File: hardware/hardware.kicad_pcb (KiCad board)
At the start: 2 copper layers, 12 parts, among them J1 Conn_01x04_Male, J2 Teensy3.2, J3 DIN-5_180degree, J4 TeensyAudioShield3.2, J5 DIN-5_180degree, U1 6N139

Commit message: Prototype layout for pcb
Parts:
- moved J3 82.4 mm to (85.0, 77.0), turned to 270 degrees
- moved J1 78.2 mm to (90.0, 97.0)
- moved R1 71.0 mm to (78.0, 85.0), turned to 90 degrees
- moved D1 60.0 mm to (81.0, 109.0)
- moved R3 54.2 mm to (53.0, 124.0), turned to 180 degrees
- moved J5 53.5 mm to (85.0, 113.0), turned to 270 degrees
- moved R2 49.1 mm to (43.0, 120.0)
- moved R4 38.6 mm to (78.0, 111.0), turned to 270 degrees
- moved U1 37.0 mm to (85.0, 105.0), turned to 180 degrees
- moved J2 34.4 mm to (56.8, 121.9)
- moved J4 34.2 mm to (56.8, 90.7)
- moved C1 23.7 mm to (78.0, 129.0), turned to 90 degrees
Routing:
- net +5V: track 0.00 -> 87.9 mm
- net /MIDI_IN: track 0.00 -> 83.7 mm
- net /SDA: track 0.00 -> 81.0 mm
- net +3V3: track 0.00 -> 74.7 mm
- net /SCL: track 0.00 -> 70.3 mm
- net /SDCS: track 0.00 -> 32.6 mm
- net /SCK: track 0.00 -> 32.6 mm
- net /DOUT: track 0.00 -> 32.6 mm
- net /DIN: track 0.00 -> 32.5 mm
- net GNDA: track 0.00 -> 32.0 mm
- net GND: track 0.00 -> 32.0 mm
- net /Vol: track 0.00 -> 32.0 mm
- net /MOSI: track 0.00 -> 32.0 mm
- net /MISO: track 0.00 -> 32.0 mm
- net /MEMCS: track 0.00 -> 32.0 mm
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- added copper zone on B.Cu, net GND
- added copper zone on F.Cu, net GND
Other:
- board outline added: 60 x 59 mm

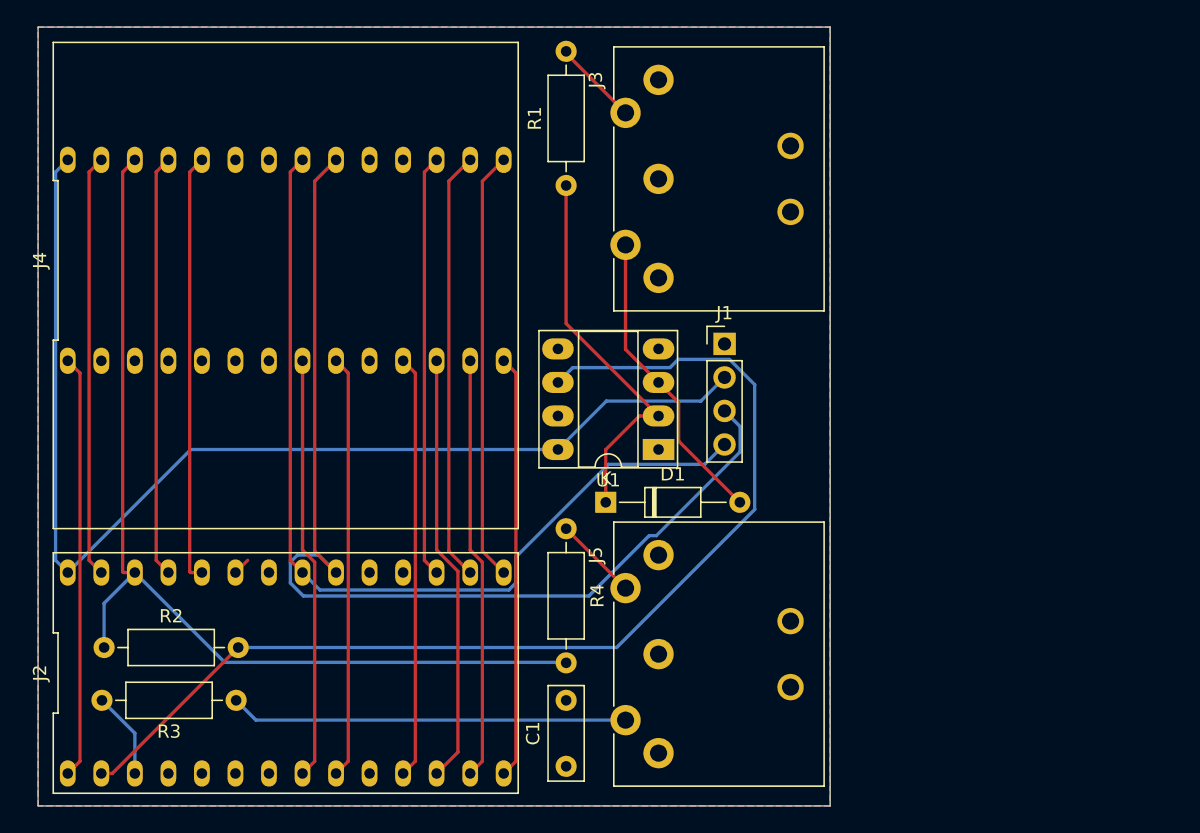
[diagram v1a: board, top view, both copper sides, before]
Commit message: Add some buttons and pots
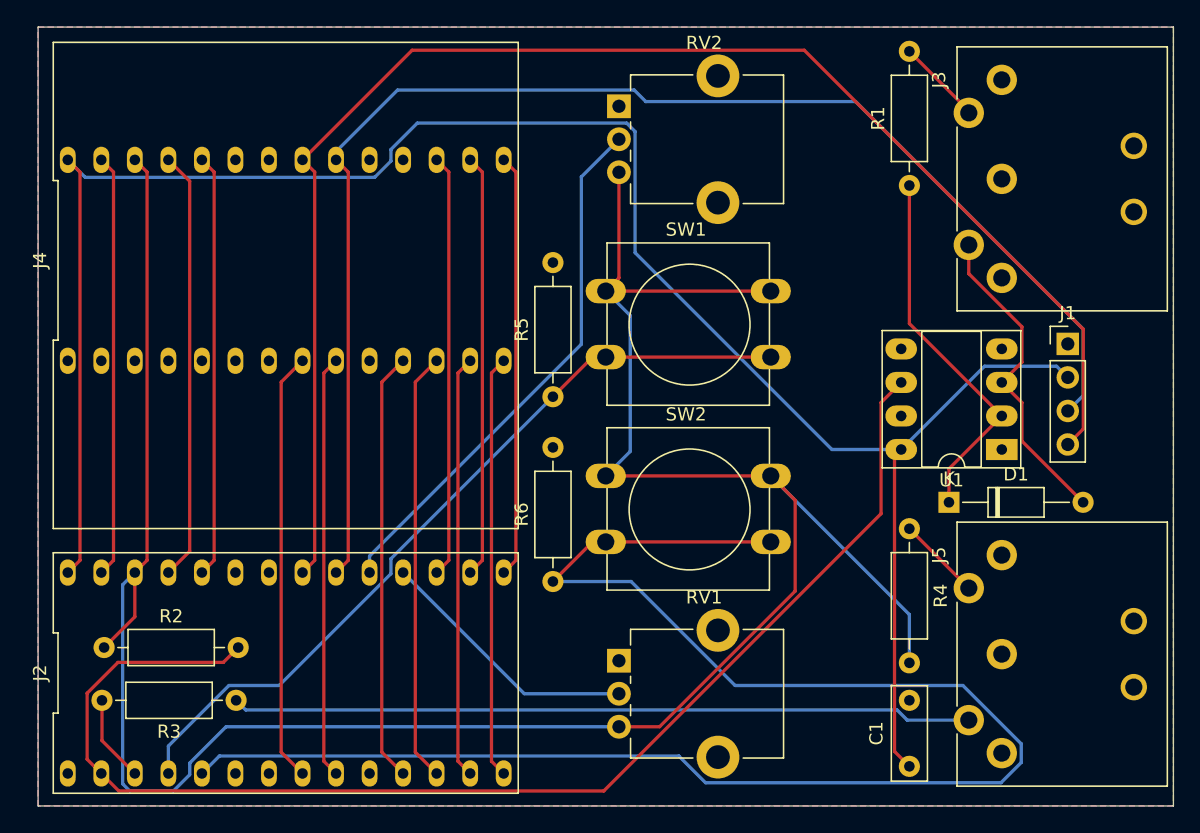
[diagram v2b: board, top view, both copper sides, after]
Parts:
- added R5: 10k, Resistor_THT:R_Axial_DIN0207_L6.3mm_D2.5mm_P10.16mm_Horizontal, F.Cu at (77.0, 101.0)
- added R6: 10k, Resistor_THT:R_Axial_DIN0207_L6.3mm_D2.5mm_P10.16mm_Horizontal, F.Cu at (77.0, 115.0)
- added RV1: R_POT, Potentiometer_THT:Potentiometer_Alpha_RD901F-40-00D_Single_Vertical_CircularHoles, F.Cu at (82.0, 121.0)
- added RV2: R_POT, Potentiometer_THT:Potentiometer_Alpha_RD901F-40-00D_Single_Vertical_CircularHoles, F.Cu at (82.0, 79.0)
- added SW1: SW_Push, Button_Switch_THT:SW_PUSH-12mm, F.Cu at (81.0, 93.0)
- added SW2: SW_Push, Button_Switch_THT:SW_PUSH-12mm, F.Cu at (81.0, 107.0)
- moved C1 26.0 mm to (104.0, 129.0)
- moved D1 26.0 mm to (107.0, 109.0)
- moved J1 26.0 mm to (116.0, 97.0)
- moved J3 26.0 mm to (111.0, 77.0)
- moved J5 26.0 mm to (111.0, 113.0)
- moved R1 26.0 mm to (104.0, 85.0)
- moved R4 26.0 mm to (104.0, 111.0)
- moved U1 26.0 mm to (111.0, 105.0)
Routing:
- net /D3: track 0.00 -> 123.8 mm
- net +3V3: track 74.7 -> 191.0 mm
- net +5V: track 87.9 -> 153.8 mm
- net /D2: track 0.00 -> 60.6 mm
- net /SCL: track 70.3 -> 112.6 mm
- net /A3: track 0.00 -> 40.6 mm
- net GND: track 32.0 -> 0.00 mm
- net Net-(J5-Pad5): track 30.1 -> 56.1 mm
- net /SDA: track 81.0 -> 105.4 mm
- net /A2: track 0.00 -> 20.2 mm
- net /MIDI_IN: track 83.7 -> 98.3 mm
- net /A7: track 1.31 -> 0.00 mm
- net Net-(D1-Pad2): track 23.1 -> 24.4 mm
- net Net-(D1-Pad1): track 29.4 -> 28.6 mm
- net /SCK: track 32.6 -> 32.0 mm
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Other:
- board size 60 x 59 mm -> 86 x 59 mm

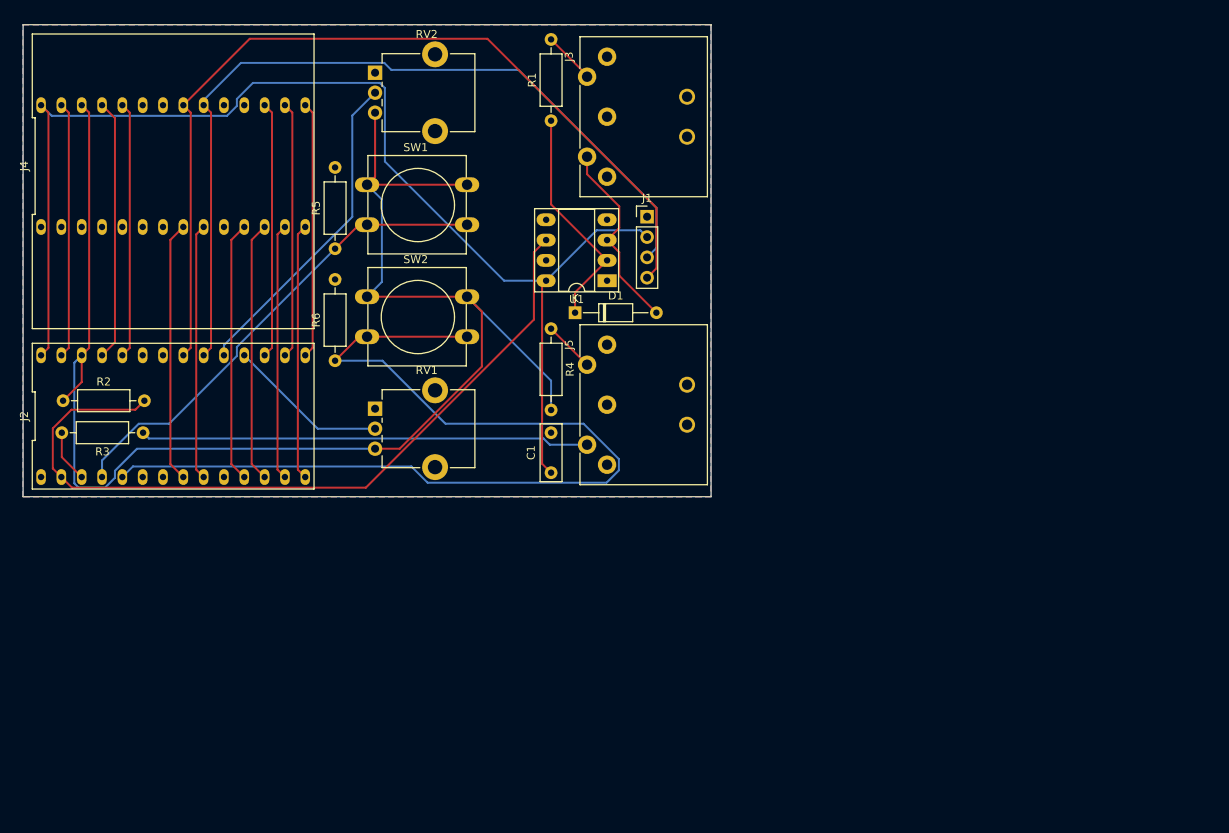
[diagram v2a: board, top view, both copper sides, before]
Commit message: Add multiplexer and update pcb
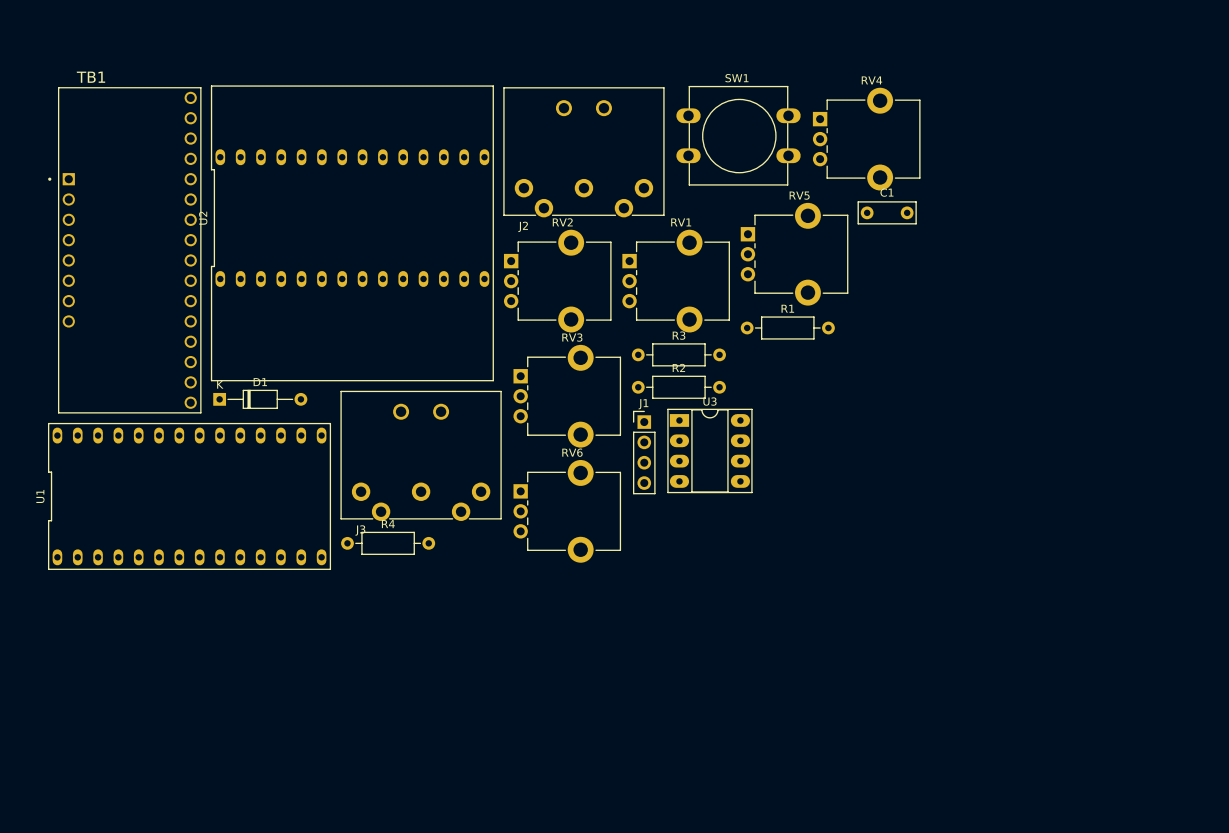
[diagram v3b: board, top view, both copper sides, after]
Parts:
- removed J4: TeensyAudioShield3.2, hardware:TeensyArduinoShield3.2
- removed J5: DIN-5_180degree, hardware:SDS-50J
- removed R5, R6: 10k, Resistor_THT:R_Axial_DIN0207_L6.3mm_D2.5mm_P10.16mm_Horizontal
- removed SW2: SW_Push, Button_Switch_THT:SW_PUSH-12mm
- added RV3: R_POT, Potentiometer_THT:Potentiometer_Alpha_RD901F-40-00D_Single_Vertical_CircularHoles, F.Cu at (100.2, 116.9)
- added RV4: R_POT, Potentiometer_THT:Potentiometer_Alpha_RD901F-40-00D_Single_Vertical_CircularHoles, F.Cu at (137.6, 84.8)
- added RV5: R_POT, Potentiometer_THT:Potentiometer_Alpha_RD901F-40-00D_Single_Vertical_CircularHoles, F.Cu at (128.6, 99.2)
- added RV6: R_POT, Potentiometer_THT:Potentiometer_Alpha_RD901F-40-00D_Single_Vertical_CircularHoles, F.Cu at (100.2, 131.3)
- added TB1: BOB-09056, BOB-09056:XDCR_BOB-09056, F.Cu at (51.3, 101.2)
- added U2: TeensyAudioShield3.2, hardware:TeensyArduinoShield3.2, F.Cu at (79.2, 97.2)
- added U3: 6N139, Package_DIP:DIP-8_W7.62mm_Socket_LongPads, F.Cu at (120.0, 122.5)
- J2: value Teensy3.2 -> DIN-5_180degree; footprint hardware:Teensy3.2 -> hardware:SDS-50J
- U1: value 6N139 -> Teensy3.2; footprint Package_DIP:DIP-8_W7.62mm_Socket_LongPads -> hardware:Teensy3.2
- moved R2 71.9 mm to (114.9, 118.3)
- moved R3 62.7 mm to (114.9, 114.3), turned to 0 degrees
- moved J3 62.5 mm to (80.2, 131.4), turned to 0 degrees
- moved U1 58.7 mm to (58.8, 132.0), turned to 0 degrees
- moved J2 52.3 mm to (100.6, 93.4)
- moved C1 51.1 mm to (143.5, 96.5), turned to 0 degrees
- moved D1 45.7 mm to (62.6, 119.8)
- moved SW1 41.1 mm to (121.2, 84.4)
- moved R4 37.0 mm to (78.5, 137.8), turned to 0 degrees
- moved RV1 36.8 mm to (113.8, 102.5)
- moved R1 35.7 mm to (128.5, 110.9), turned to 0 degrees
- moved RV2 29.1 mm to (99.0, 102.5)
- moved J1 25.7 mm to (115.7, 122.7)
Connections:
- J2 pad 1: GND -> Net-(J2-Pad1)
- J2 pad 2: /MIDI_IN -> Net-(J2-Pad2)
- J2 pad 3: /MIDI_OUT -> Net-(J2-Pad3)
- J2 pad 4: /D2 -> Net-(J2-Pad4)
- J2 pad 5: /D3 -> Net-(D1-Pad2)
- J3 pad 2: Net-(J3-Pad2) -> GND
- J3 pad 5: Net-(D1-Pad2) -> Net-(J3-Pad5)
- R1 pad 2: Net-(J3-Pad4) -> Net-(J2-Pad4)
- R3 pad 1: Net-(J5-Pad5) -> Net-(J3-Pad5)
- R4 pad 1: Net-(J5-Pad4) -> Net-(J3-Pad4)
- RV1 pad 2: /A2 -> /Filter_Freq
- RV2 pad 2: /A3 -> /Filter_Res
- SW1 pad 2: /D2 -> /OSC1_WAV
- U1 pad 1: Net-(U1-Pad1) -> GND
- U1 pad 2: Net-(D1-Pad1) -> /MIDI_IN
- U1 pad 3: Net-(D1-Pad2) -> /MIDI_OUT
- U1 pad 4: Net-(U1-Pad4) -> /D2
- U1 pad 5: GND -> /D3
- U1 pad 6: /MIDI_IN -> /D4
- U1 pad 7: Net-(U1-Pad7) -> /D5
- U1 pad 8: +5V -> /MEMCS
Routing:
- net +3V3: track 191.0 -> 0.00 mm
- net +5V: track 153.8 -> 0.00 mm
- net /D3: track 123.8 -> 0.00 mm
- net /SCL: track 112.6 -> 0.00 mm
- net /SDA: track 105.4 -> 0.00 mm
- net /MIDI_IN: track 98.3 -> 0.00 mm
- net /D2: track 60.6 -> 0.00 mm
- net Net-(J5-Pad5): track 56.1 -> 0.00 mm
- net /A3: track 40.6 -> 0.00 mm
- net /LRCLK: track 32.6 -> 0.00 mm
- net /BCLK: track 32.6 -> 0.00 mm
- net /MEMCS: track 32.6 -> 0.00 mm
- net /SDCS: track 32.6 -> 0.00 mm
- net GNDA: track 32.0 -> 0.00 mm
- net /Vol: track 32.0 -> 0.00 mm
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- removed copper zone on B.Cu, net GND
- removed copper zone on F.Cu, net GND
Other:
- board outline removed

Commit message: Layout pcb
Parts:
- moved J3 93.8 mm to (174.0, 134.6), turned to 270 degrees
- moved U2 79.0 mm to (147.3, 137.2), turned to 90 degrees
- moved D1 76.0 mm to (138.4, 115.6)
- moved J2 73.4 mm to (174.0, 96.5), turned to 270 degrees
- moved U1 60.8 mm to (119.4, 137.2), turned to 90 degrees
- moved RV6 58.9 mm to (152.4, 104.1), turned to 90 degrees
- moved TB1 58.3 mm to (99.1, 134.6), turned to 180 degrees
- moved U3 54.0 mm to (174.0, 120.7)
- moved RV2 53.7 mm to (76.2, 151.1), turned to 90 degrees
- moved SW1 49.7 mm to (72.4, 94.0)
- moved RV1 44.9 mm to (76.2, 127.0), turned to 90 degrees
- moved C1 42.1 mm to (180.3, 116.8), turned to 180 degrees
- moved R4 41.2 mm to (110.5, 111.8)
- moved RV4 30.3 mm to (114.3, 104.1), turned to 90 degrees
- moved J1 26.6 mm to (92.7, 109.2), turned to 90 degrees
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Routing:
- net +3V3: track 0.00 -> 233.6 mm
- net +5V: track 0.00 -> 156.0 mm
- net /ADSR_Sustain: track 0.00 -> 105.5 mm
- net /MIDI_IN: track 0.00 -> 101.7 mm
- net /ADSR_Release: track 0.00 -> 98.7 mm
- net Net-(J3-Pad5): track 0.00 -> 81.8 mm
- net Net-(J3-Pad4): track 0.00 -> 72.8 mm
- net /ADSR_Decay: track 0.00 -> 65.0 mm
- net /SCL: track 0.00 -> 60.1 mm
- net /SDA: track 0.00 -> 59.0 mm
- net Net-(D1-Pad1): track 0.00 -> 55.2 mm
- net /OSC1_WAV: track 0.00 -> 54.7 mm
- net /ADSR_Attack: track 0.00 -> 51.8 mm
- net Net-(D1-Pad2): track 0.00 -> 44.6 mm
- net Net-(J2-Pad4): track 0.00 -> 42.1 mm
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- added copper zone on B.Cu, net GND
- added copper zone on F.Cu, net GND
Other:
- board outline added: 116.8 x 67.3 mm
